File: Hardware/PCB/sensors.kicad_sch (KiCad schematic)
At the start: 16 parts, among them IC1 MPXV6115VC6U, IC2 MPX5100GP, U2 ADS1219IPWR, U3 LP3987H-33B5

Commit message: added a lot of stuff, going to work on LCD + Touch next
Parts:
- C1: value 0.01u -> 0.01uF
- C12, C13, C2, C5: value 1u -> 1uF
- C4: value 47p -> 47pF
- C6: value 100n -> 100nF
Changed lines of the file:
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@@
 			)
 		)
-		(property "Value" "1u"
+		(property "Value" "1uF"
 			(at 181.61 116.8338 0)
 			(effects
@@
 			)
 		)
-		(property "Value" "0.01u"
+		(property "Value" "0.01uF"
 			(at 90.17 111.7662 0)
 			(effects
@@
 			)
 		)
-		(property "Value" "47p"
+		(property "Value" "47pF"
 			(at 80.01 39.3635 0)
 			(effects
@@
 			)
 		)
-		(property "Value" "1u"
+		(property "Value" "1uF"
 			(at 146.05 116.8338 0)
 			(effects
@@
 			)
 		)
-		(property "Value" "1u"
+		(property "Value" "1uF"
 			(at 74.93 50.7938 0)
 			(effects
@@
 			)
 		)
-		(property "Value" "100n"
+		(property "Value" "100nF"
 			(at 90.17 53.3335 0)
 			(effects
@@
 			)
 		)
-		(property "Value" "1u"
+		(property "Value" "1uF"
 			(at 81.28 111.7662 0)
 			(effects

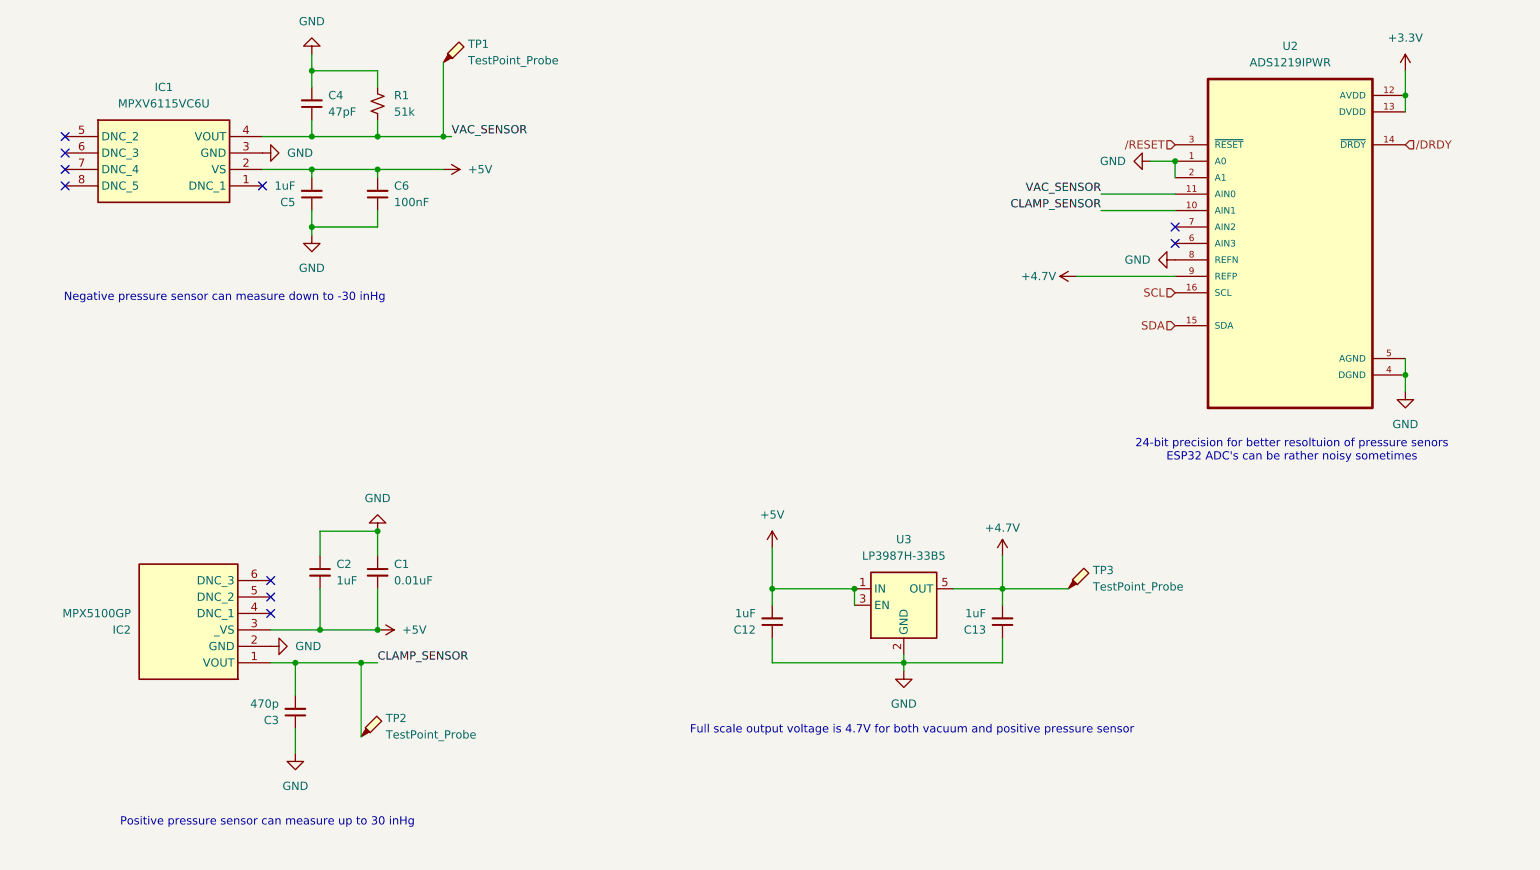
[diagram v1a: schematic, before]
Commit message: switched to making buck converter to save costs and space, and to allow for LDO after 5.5V for better stability
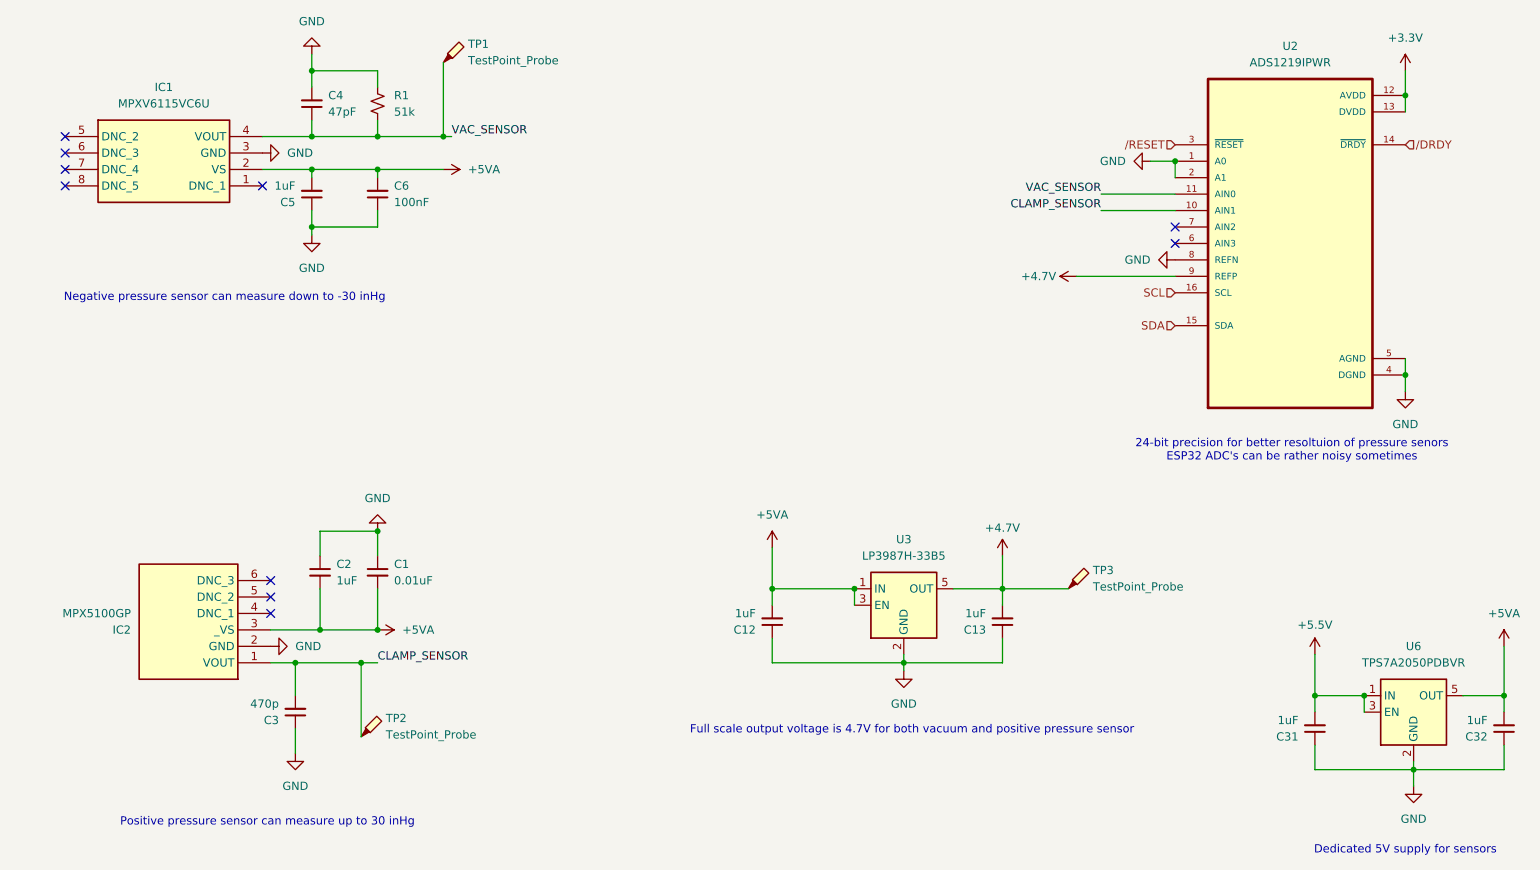
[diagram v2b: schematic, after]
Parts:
- added C31, C32: 1uF, Capacitor_SMD:C_0603_1608Metric_Pad1.08x0.95mm_HandSolder, symbol Device:C_Small
- added U6: TPS7A2050PDBVR, Package_TO_SOT_SMD:SOT-23-5, symbol Regulator_Linear:TPS7A0531PDBV
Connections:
- net GND: now also C31.1, C32.1, U6.2 (GND)
- net +5V renamed +5VA
- net +5VA: now also C32.2, U6.5 (OUT)
- new net +5.5V: C31.2, U6.1 (IN), U6.3 (EN)
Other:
- note added: "Dedicated 5V supply for sensors"

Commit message: swapped to be better precision resistors for feedback on buck and votlage reference for ADCs
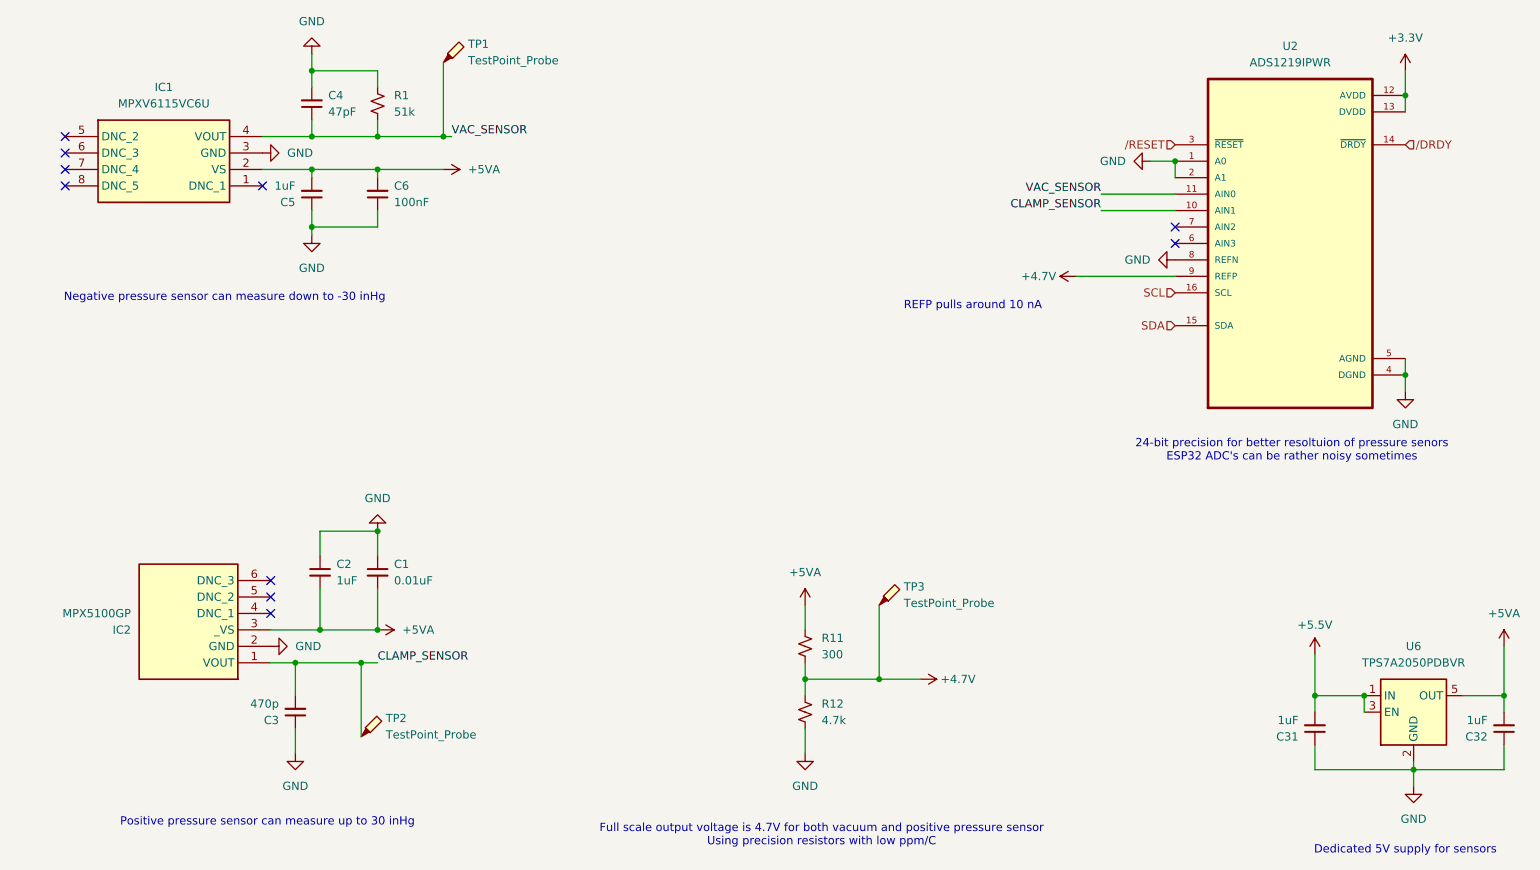
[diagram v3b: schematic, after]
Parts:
- removed C12, C13: 1uF, Capacitor_SMD:C_0603_1608Metric_Pad1.08x0.95mm_HandSolder, symbol Device:C_Small
- removed U3: LP3987H-33B5, Package_TO_SOT_SMD:TO-263-5_TabPin3, symbol Regulator_Linear:LP3987H-33B5
- added R11: 300, Resistor_SMD:R_0603_1608Metric_Pad0.98x0.95mm_HandSolder, symbol Device:R_Small_US
- added R12: 4.7k, Resistor_SMD:R_0603_1608Metric_Pad0.98x0.95mm_HandSolder, symbol Device:R_Small_US
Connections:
- net +4.7V: now also R11.2, R12.1
- net +5VA: now also R11.1
- net GND: now also R12.2
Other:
- note added: "Full scale output voltage is 4.7V for both vacuum and positive pressure sensor Using precision resistors with low ppm/C"
- note added: "REFP pulls around 10 nA"
- note removed: "Full scale output voltage is 4.7V for both vacuum and positive pressure sensor"

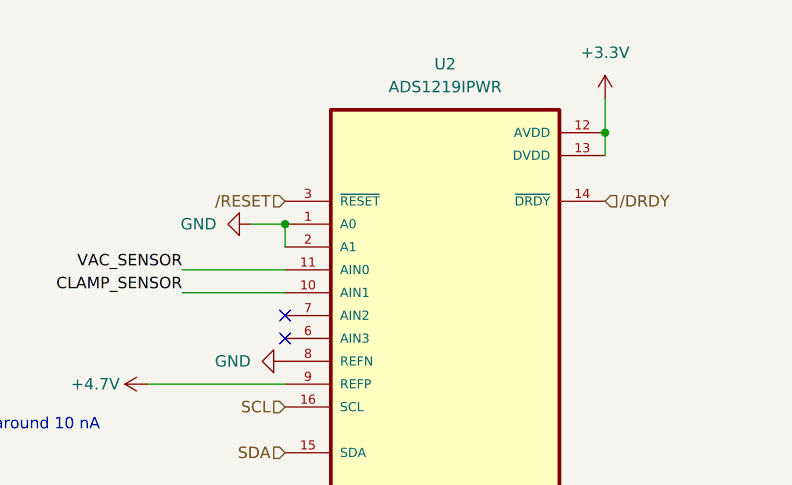
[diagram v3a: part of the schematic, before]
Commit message: overall design is pretty much done, starting layout and routing now
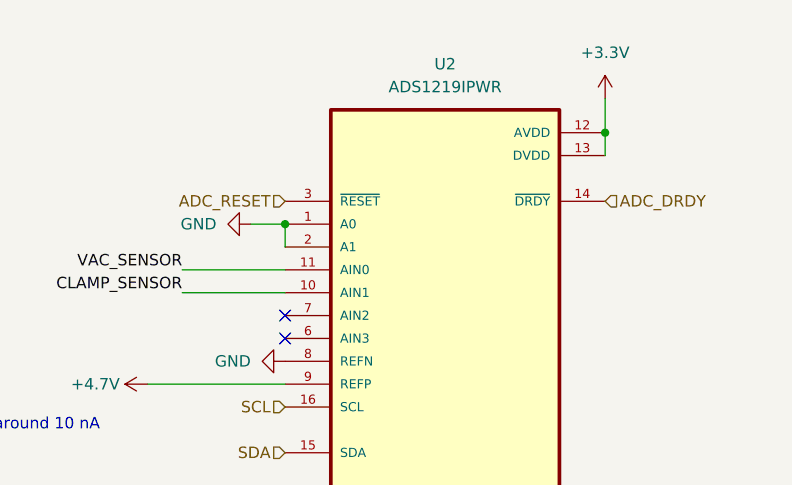
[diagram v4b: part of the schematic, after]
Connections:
- net /DRDY renamed ADC_DRDY
- net /RESET renamed ADC_RESET
